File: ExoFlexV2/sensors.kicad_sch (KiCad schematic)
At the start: 14 parts, among them J10 Screw_Terminal_01x02, J11 Screw_Terminal_01x02, J13 Screw_Terminal_01x02, J14 Screw_Terminal_01x02, J15 Screw_Terminal_01x02, J17 Screw_Terminal_5V, J19 Screw_Terminal_GND, J8 Screw_Terminal_01x02, J9 Screw_Terminal_01x02, U10 Switch(5A), U11 Switch(5A), U12 Switch(5A), U8 MPU6050_acc_gyro, U9 MPU6050_acc_gyro

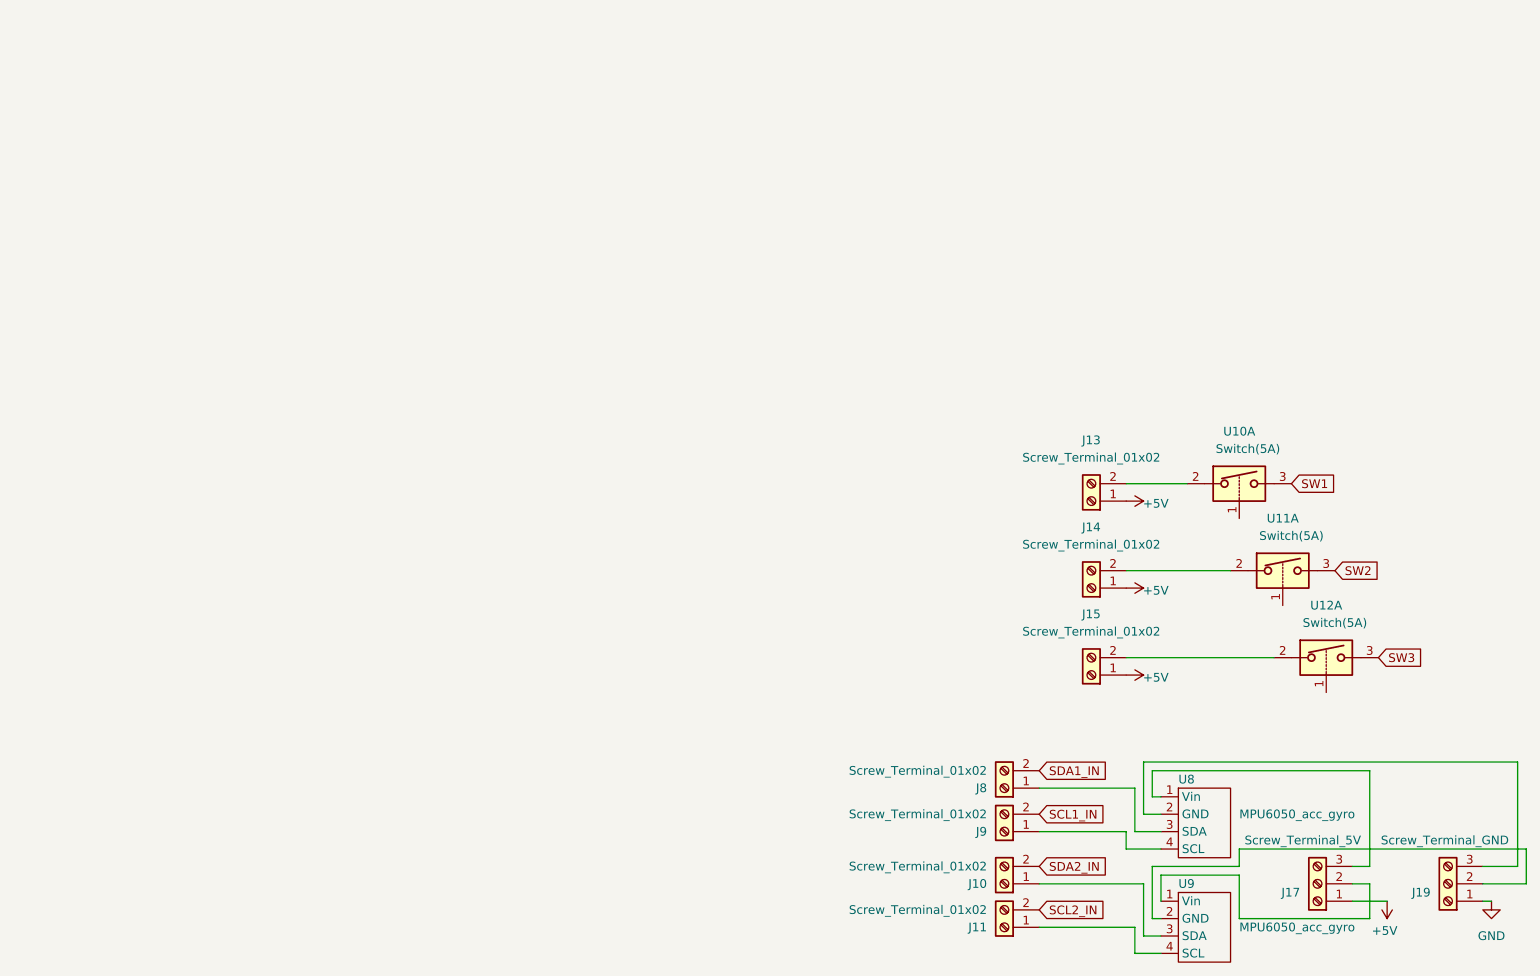
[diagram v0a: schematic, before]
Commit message: Ajout des capteurs de courant, loadcell et potentiomètre et remplacement du stm32 par Raspberry Pi 4
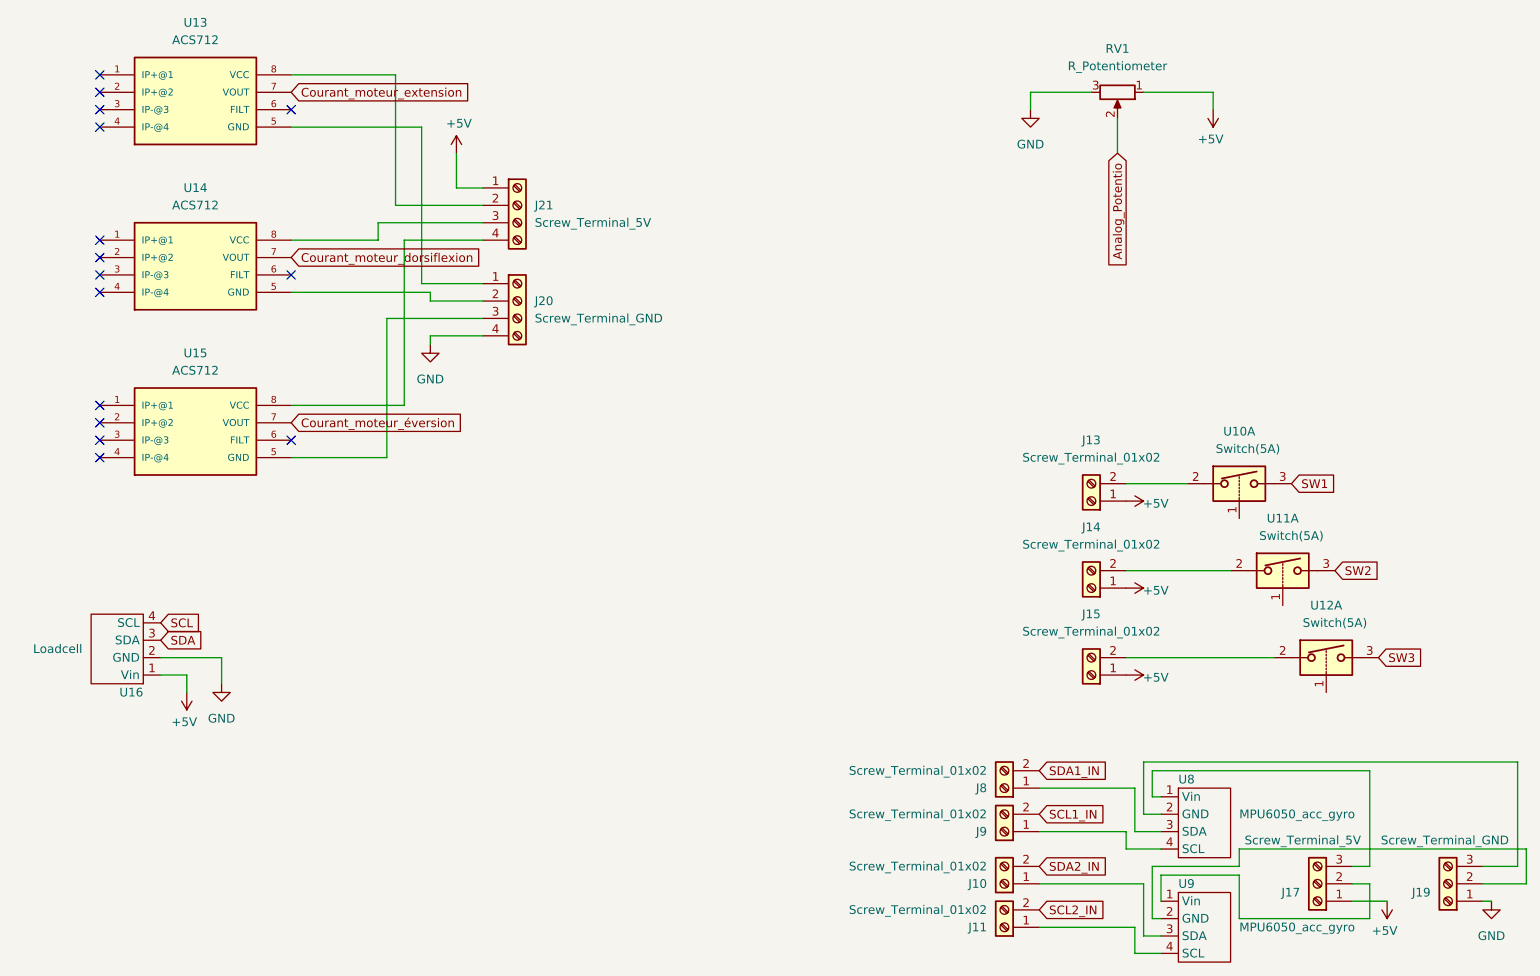
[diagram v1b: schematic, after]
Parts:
- added J20: Screw_Terminal_GND, symbol Connector:Screw_Terminal_01x04
- added J21: Screw_Terminal_5V, symbol Connector:Screw_Terminal_01x04
- added RV1: R_Potentiometer, symbol Device:R_Potentiometer
- added U13, U14, U15: ACS712, ACS712:SO08, symbol ACS712:ACS712
- added U16: Loadcell, symbol Sensor_library:MPU6050_acc_gyro
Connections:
- net +5V: now also J21.1 (Pin_1), RV1.1, U16.1 (Vin)
- net GND: now also J20.4 (Pin_4), RV1.3, U16.2 (GND)
- new net: J20.1 (Pin_1), U13.5 (GND)
- new net: J20.2 (Pin_2), U14.5 (GND)
- new net: J20.3 (Pin_3), U15.5 (GND)
- new net: J21.2 (Pin_2), U13.8 (VCC)
- new net: J21.3 (Pin_3), U14.8 (VCC)
- new net: J21.4 (Pin_4), U15.8 (VCC)
- new net Analog_Potentio: RV1.2
- new net Courant_moteur_dorsiflexion: U14.7 (VOUT)
- new net Courant_moteur_extension: U13.7 (VOUT)
- new net Courant_moteur_éversion: U15.7 (VOUT)
- new net SCL: U16.4 (SCL)
- new net SDA: U16.3 (SDA)
- no-connect marks 0 -> 15
